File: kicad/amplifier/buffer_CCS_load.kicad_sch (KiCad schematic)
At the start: 3 parts, among them Q9 DN2540

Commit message: cleanup
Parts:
- renumbered Q9 to Q10, R40 to R42, R41 to R43
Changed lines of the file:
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@@
 		(on_board yes)
 		(dnp no)
-		(property "Reference" "R41"
+		(property "Reference" "R43"
 			(at 134.62 97.79 90)
 			(effects
@@
 		(on_board yes)
 		(dnp no)
-		(property "Reference" "R40"
+		(property "Reference" "R42"
 			(at 125.73 87.63 90)
 			(effects
@@
 		(on_board yes)
 		(dnp no)
-		(property "Reference" "Q9"
+		(property "Reference" "Q10"
 			(at 139.7 85.09 0)
 			(effects

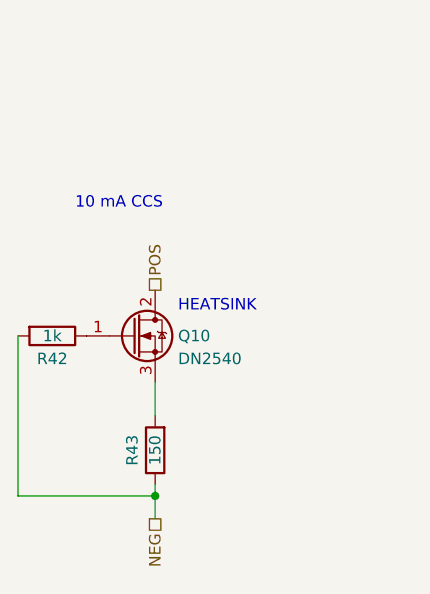
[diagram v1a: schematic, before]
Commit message: add diode to protect FET drain pin in buffer CCS from negative drain-source voltage (that may happen in case of large AC swings).
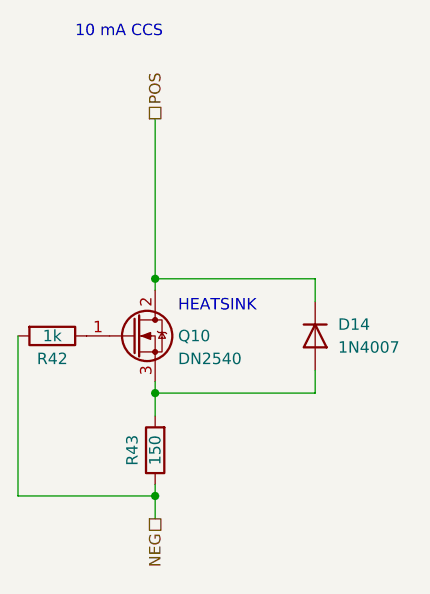
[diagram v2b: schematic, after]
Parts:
- added D14: 1N4007, Diode_THT:D_DO-41_SOD81_P10.16mm_Horizontal, symbol Diode:1N4007
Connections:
- net POS: now also D14.1 (K)
- net at Q10.3 (S), R43.2: now also D14.2 (A)
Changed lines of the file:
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@@
 	(paper "A4")
+	(junction
+		(at 137.16 78.74)
+		(diameter 0)
+		(color 0 0 0 0)
+	)
 	(junction
 		(at 137.16 102.87)
@@
 		(color 0 0 0 0)
 	)
+	(junction
+		(at 137.16 91.44)
+		(diameter 0)
+		(color 0 0 0 0)
+	)
 	(wire
 		(pts
@@
 	(wire
 		(pts
+			(xy 137.16 91.44) (xy 137.16 90.17)
+		)
+		(stroke
+			(width 0)
+			(type default)
+		)
+	)
+	(wire
+		(pts
 			(xy 121.92 85.09) (xy 121.92 102.87)
 		)
@@
 	(wire
 		(pts
+			(xy 154.94 88.9) (xy 154.94 91.44)
+		)
+		(stroke
+			(width 0)
+			(type default)
+		)
+	)
+	(wire
+		(pts
 			(xy 121.92 102.87) (xy 137.16 102.87)
 		)
@@
 	(wire
 		(pts
-			(xy 137.16 93.98) (xy 137.16 90.17)
+			(xy 137.16 60.96) (xy 137.16 78.74)
+		)
+		(stroke
+			(width 0)
+			(type default)
+		)
+	)
+	(wire
+		(pts
+			(xy 154.94 91.44) (xy 137.16 91.44)
+		)
+		(stroke
+			(width 0)
+			(type default)
+		)
+	)
+	(wire
+		(pts
+			(xy 137.16 78.74) (xy 137.16 80.01)
+		)
+		(stroke
+			(width 0)
+			(type default)
+		)
+	)
+	(wire
+		(pts
+			(xy 137.16 93.98) (xy 137.16 91.44)
+		)
+		(stroke
+			(width 0)
+			(type default)
+		)
+	)
+	(wire
+		(pts
+			(xy 154.94 78.74) (xy 137.16 78.74)
+		)
+		(stroke
+			(width 0)
+			(type default)
+		)
+	)
+	(wire
+		(pts
+			(xy 154.94 81.28) (xy 154.94 78.74)
 		)
 		(stroke
@@
 	(text "10 mA CCS"
 		(exclude_from_sim no)
-		(at 128.27 71.12 0)
+		(at 128.27 52.07 0)
 		(effects
 			(font
@@
 	(hierarchical_label "POS"
 		(shape passive)
-		(at 137.16 80.01 90)
+		(at 137.16 60.96 90)
 		(fields_autoplaced yes)
 		(effects
@@
 					(unit 1)
 				)
+			)
+		)
+	)
+	(symbol
+		(lib_id "Diode:1N4007")
+		(at 154.94 85.09 270)
+		(unit 1)
+		(exclude_from_sim no)
+		(in_bom yes)
+		(on_board yes)
+		(dnp no)
+		(fields_autoplaced yes)
+		(property "Reference" "D14"
+			(at 157.48 83.8199 90)
+			(effects
+				(font
+					(size 1.27 1.27)
+				)
+				(justify left)
+			)
+		)
+		(property "Value" "1N4007"
+			(at 157.48 86.3599 90)
+			(effects
+				(font
+					(size 1.27 1.27)
+				)
+				(justify left)
+			)
+		)
+		(property "Footprint" "Diode_THT:D_DO-41_SOD81_P10.16mm_Horizontal"
+			(at 150.495 85.09 0)
+			(effects
+				(font
+					(size 1.27 1.27)
+				)
+				(hide yes)
+			)
+		)
+		(property "Datasheet" "http://www.vishay.com/docs/88503/1n4001.pdf"
+			(at 154.94 85.09 0)
+			(effects
+				(font
+					(size 1.27 1.27)
+				)
+				(hide yes)
+			)
+		)
+		(property "Description" "1000V 1A General Purpose Rectifier Diode, DO-41"
+			(at 154.94 85.09 0)
+			(effects
+				(font
+					(size 1.27 1.27)
+				)
+				(hide yes)
+			)
+		)
+		(property "Sim.Device" "D"
+			(at 154.94 85.09 0)
+			(effects
+				(font
+					(size 1.27 1.27)
+				)
+				(hide yes)
+			)
+		)
+		(property "Sim.Pins" "1=K 2=A"
+			(at 154.94 85.09 0)
+			(effects
+				(font
+					(size 1.27 1.27)
+				)
+				(hide yes)
+			)
+		)
+		(pin "1"
+		)
+		(pin "2"
+		)
+		(instances
+			(project ""
+				(path "/59cc4414-299b-49db-9f9a-b06f69a12073/117f0db4-f368-407f-8708-b67954482099"
+					(reference "D14")
+					(unit 1)
+				)
+				(path "/59cc4414-299b-49db-9f9a-b06f69a12073/964c5f27-279d-4094-beed-423757c37563"
+					(reference "D13")
+					(unit 1)
+				)

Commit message: design notes for mu-stage
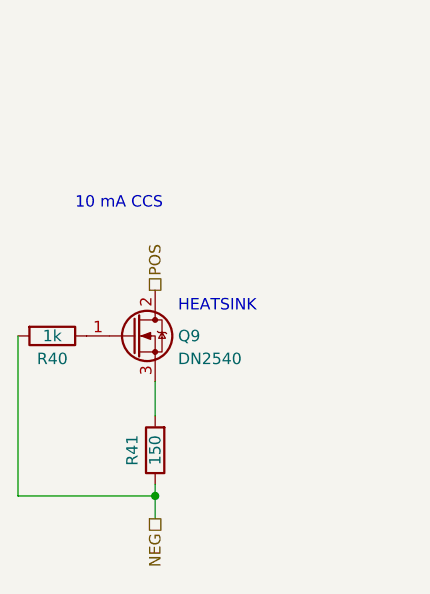
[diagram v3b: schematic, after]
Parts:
- removed D14: 1N4007, Diode_THT:D_DO-41_SOD81_P10.16mm_Horizontal, symbol Diode:1N4007
- renumbered Q10 to Q9, R42 to R40, R43 to R41
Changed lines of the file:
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@@
 	(paper "A4")
-	(junction
-		(at 137.16 78.74)
-		(diameter 0)
-		(color 0 0 0 0)
-	)
 	(junction
 		(at 137.16 102.87)
@@
 		(color 0 0 0 0)
 	)
-	(junction
-		(at 137.16 91.44)
-		(diameter 0)
-		(color 0 0 0 0)
-	)
 	(wire
 		(pts
@@
 	(wire
 		(pts
-			(xy 137.16 91.44) (xy 137.16 90.17)
-		)
-		(stroke
-			(width 0)
-			(type default)
-		)
-	)
-	(wire
-		(pts
 			(xy 121.92 85.09) (xy 121.92 102.87)
 		)
@@
 	(wire
 		(pts
-			(xy 154.94 88.9) (xy 154.94 91.44)
-		)
-		(stroke
-			(width 0)
-			(type default)
-		)
-	)
-	(wire
-		(pts
 			(xy 121.92 102.87) (xy 137.16 102.87)
 		)
@@
 	(wire
 		(pts
-			(xy 137.16 60.96) (xy 137.16 78.74)
-		)
-		(stroke
-			(width 0)
-			(type default)
-		)
-	)
-	(wire
-		(pts
-			(xy 154.94 91.44) (xy 137.16 91.44)
-		)
-		(stroke
-			(width 0)
-			(type default)
-		)
-	)
-	(wire
-		(pts
-			(xy 137.16 78.74) (xy 137.16 80.01)
-		)
-		(stroke
-			(width 0)
-			(type default)
-		)
-	)
-	(wire
-		(pts
-			(xy 137.16 93.98) (xy 137.16 91.44)
-		)
-		(stroke
-			(width 0)
-			(type default)
-		)
-	)
-	(wire
-		(pts
-			(xy 154.94 78.74) (xy 137.16 78.74)
-		)
-		(stroke
-			(width 0)
-			(type default)
-		)
-	)
-	(wire
-		(pts
-			(xy 154.94 81.28) (xy 154.94 78.74)
+			(xy 137.16 93.98) (xy 137.16 90.17)
 		)
 		(stroke
@@
 	(text "10 mA CCS"
 		(exclude_from_sim no)
-		(at 128.27 52.07 0)
+		(at 128.27 71.12 0)
 		(effects
 			(font
@@
 	(hierarchical_label "POS"
 		(shape passive)
-		(at 137.16 60.96 90)
+		(at 137.16 80.01 90)
 		(fields_autoplaced yes)
 		(effects
@@
 		(on_board yes)
 		(dnp no)
-		(property "Reference" "R43"
+		(property "Reference" "R41"
 			(at 134.62 97.79 90)
 			(effects
@@
 		(instances
 			(project "OSDEHA_AMP"
+				(path "/59cc4414-299b-49db-9f9a-b06f69a12073/964c5f27-279d-4094-beed-423757c37563"
+					(reference "R41")
+					(unit 1)
+				)
 				(path "/59cc4414-299b-49db-9f9a-b06f69a12073/117f0db4-f368-407f-8708-b67954482099"
 					(reference "R43")
-					(unit 1)
-				)
-				(path "/59cc4414-299b-49db-9f9a-b06f69a12073/964c5f27-279d-4094-beed-423757c37563"
-					(reference "R41")
 					(unit 1)
 				)
@@
 		(on_board yes)
 		(dnp no)
-		(property "Reference" "R42"
+		(property "Reference" "R40"
 			(at 125.73 87.63 90)
 			(effects
@@
 		(instances
 			(project "OSDEHA_AMP"
+				(path "/59cc4414-299b-49db-9f9a-b06f69a12073/964c5f27-279d-4094-beed-423757c37563"
+					(reference "R40")
+					(unit 1)
+				)
 				(path "/59cc4414-299b-49db-9f9a-b06f69a12073/117f0db4-f368-407f-8708-b67954482099"
 					(reference "R42")
-					(unit 1)
-				)
-				(path "/59cc4414-299b-49db-9f9a-b06f69a12073/964c5f27-279d-4094-beed-423757c37563"
-					(reference "R40")
-					(unit 1)
-				)
-			)
-		)
-	)
-	(symbol
-		(lib_id "Diode:1N4007")
-		(at 154.94 85.09 270)
-		(unit 1)
-		(exclude_from_sim no)
-		(in_bom yes)
-		(on_board yes)
-		(dnp no)
-		(fields_autoplaced yes)
-		(property "Reference" "D14"
-			(at 157.48 83.8199 90)
-			(effects
-				(font
-					(size 1.27 1.27)
-				)
-				(justify left)
-			)
-		)
-		(property "Value" "1N4007"
-			(at 157.48 86.3599 90)
-			(effects
-				(font
-					(size 1.27 1.27)
-				)
-				(justify left)
-			)
-		)
-		(property "Footprint" "Diode_THT:D_DO-41_SOD81_P10.16mm_Horizontal"
-			(at 150.495 85.09 0)
-			(effects
-				(font
-					(size 1.27 1.27)
-				)
-				(hide yes)
-			)
-		)
-		(property "Datasheet" "http://www.vishay.com/docs/88503/1n4001.pdf"
-			(at 154.94 85.09 0)
-			(effects
-				(font
-					(size 1.27 1.27)
-				)
-				(hide yes)
-			)
-		)
-		(property "Description" "1000V 1A General Purpose Rectifier Diode, DO-41"
-			(at 154.94 85.09 0)
-			(effects
-				(font
-					(size 1.27 1.27)
-				)
-				(hide yes)
-			)
-		)
-		(property "Sim.Device" "D"
-			(at 154.94 85.09 0)
-			(effects
-				(font
-					(size 1.27 1.27)
-				)
-				(hide yes)
-			)
-		)
-		(property "Sim.Pins" "1=K 2=A"
-			(at 154.94 85.09 0)
-			(effects
-				(font
-					(size 1.27 1.27)
-				)
-				(hide yes)
-			)
-		)
-		(pin "1"
-		)
-		(pin "2"
-		)
-		(instances
-			(project ""
-				(path "/59cc4414-299b-49db-9f9a-b06f69a12073/117f0db4-f368-407f-8708-b67954482099"
-					(reference "D14")
-					(unit 1)
-				)
-				(path "/59cc4414-299b-49db-9f9a-b06f69a12073/964c5f27-279d-4094-beed-423757c37563"
-					(reference "D13")
 					(unit 1)
 				)
@@
 		(on_board yes)
 		(dnp no)
-		(property "Reference" "Q10"
+		(property "Reference" "Q9"
 			(at 139.7 85.09 0)
 			(effects
@@
 		(instances
 			(project "OSDEHA_AMP"
+				(path "/59cc4414-299b-49db-9f9a-b06f69a12073/964c5f27-279d-4094-beed-423757c37563"
+					(reference "Q9")
+					(unit 1)
+				)
 				(path "/59cc4414-299b-49db-9f9a-b06f69a12073/117f0db4-f368-407f-8708-b67954482099"
 					(reference "Q10")
 					(unit 1)
 				)
-				(path "/59cc4414-299b-49db-9f9a-b06f69a12073/964c5f27-279d-4094-beed-423757c37563"
-					(reference "Q9")
-					(unit 1)
-				)
